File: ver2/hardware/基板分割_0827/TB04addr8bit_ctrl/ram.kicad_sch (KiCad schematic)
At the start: 6 parts, among them U1101 6116, U1102 74HC244, U1103 74HC244

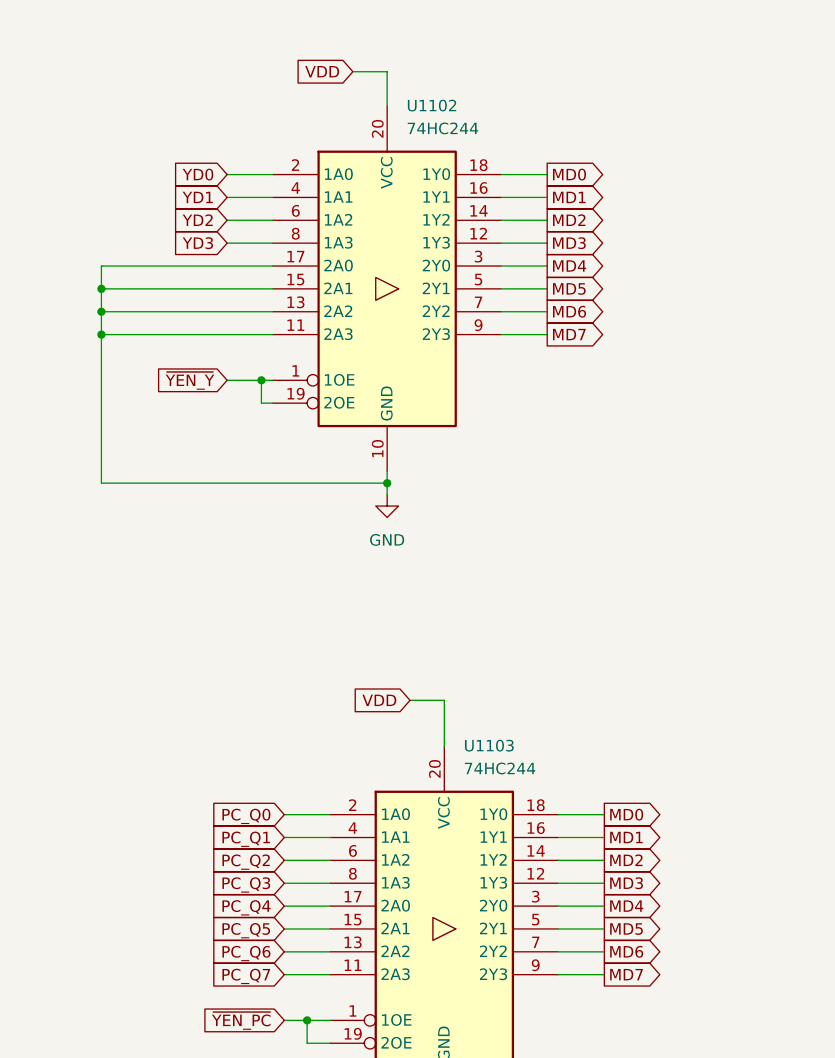
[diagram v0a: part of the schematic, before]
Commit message: ver2: 制御板のピン割当(案C)を適用(6IC・44ピン入替で交差-17.7%)
74HC244×3(U1102/U1103/U1402)・74HC157×3(U101/U401/U404)でバスのビット順を入替。
検証は全項目合格＝変化は44パッドのみ・244の(A,Y)対と157の(A,B,Y)三つ組は集合一致・
制御ピン不変・ネットの構成部品変化0・DRC/schematic parityはHEADと項目単位で完全一致。
HPWL +0.16%(15,542→15,567mm)。配置と外形は不動。

Co-Authored-By: Claude Opus 5 <noreply@anthropic.com>
Claude-Session: https://claude.ai/code/session_01FHQyZznjPPN9g6quxMNLGo
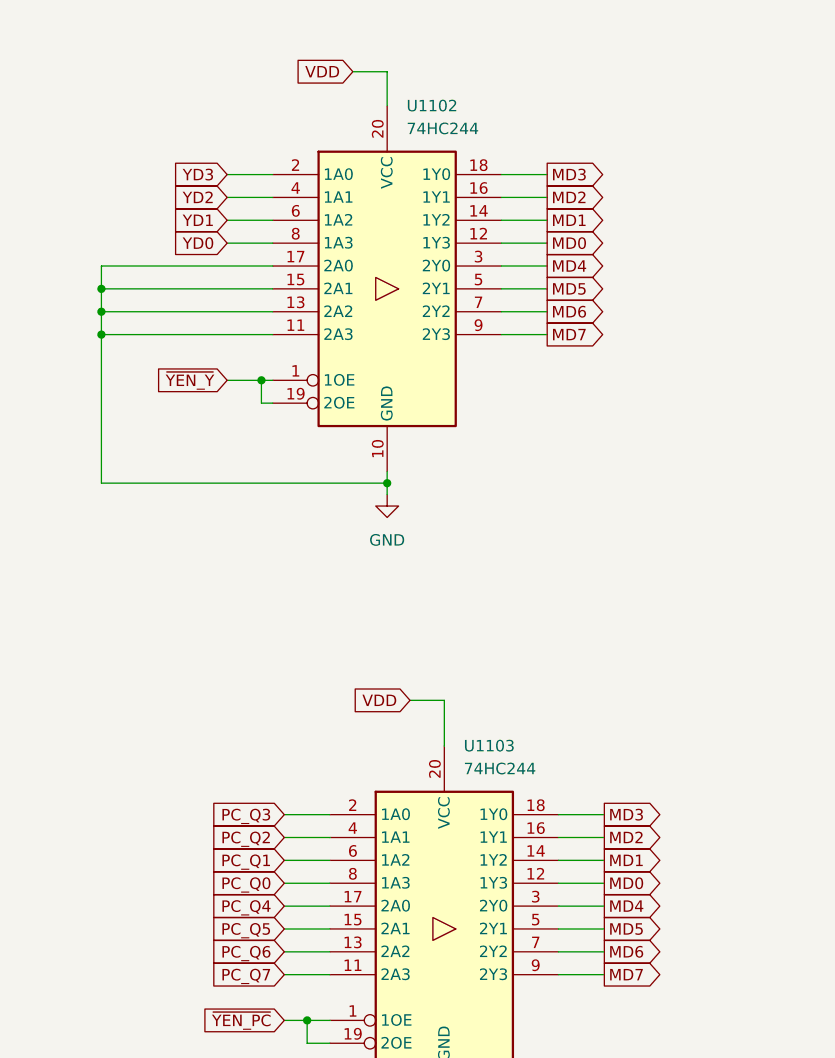
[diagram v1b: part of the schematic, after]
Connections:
- net MD0: now also U1102.12 (1Y3), U1103.12 (1Y3); no longer U1102.18 (1Y0), U1103.18 (1Y0)
- net MD1: now also U1102.14 (1Y2), U1103.14 (1Y2); no longer U1102.16 (1Y1), U1103.16 (1Y1)
- net MD2: now also U1102.16 (1Y1), U1103.16 (1Y1); no longer U1102.14 (1Y2), U1103.14 (1Y2)
- net MD3: now also U1102.18 (1Y0), U1103.18 (1Y0); no longer U1102.12 (1Y3), U1103.12 (1Y3)
- net PC_Q0: now also U1103.8 (1A3); no longer U1103.2 (1A0)
- net PC_Q1: now also U1103.6 (1A2); no longer U1103.4 (1A1)
- net PC_Q2: now also U1103.4 (1A1); no longer U1103.6 (1A2)
- net PC_Q3: now also U1103.2 (1A0); no longer U1103.8 (1A3)
- net YD0: now also U1102.8 (1A3); no longer U1102.2 (1A0)
- net YD1: now also U1102.6 (1A2); no longer U1102.4 (1A1)
- net YD2: now also U1102.4 (1A1); no longer U1102.6 (1A2)
- net YD3: now also U1102.2 (1A0); no longer U1102.8 (1A3)

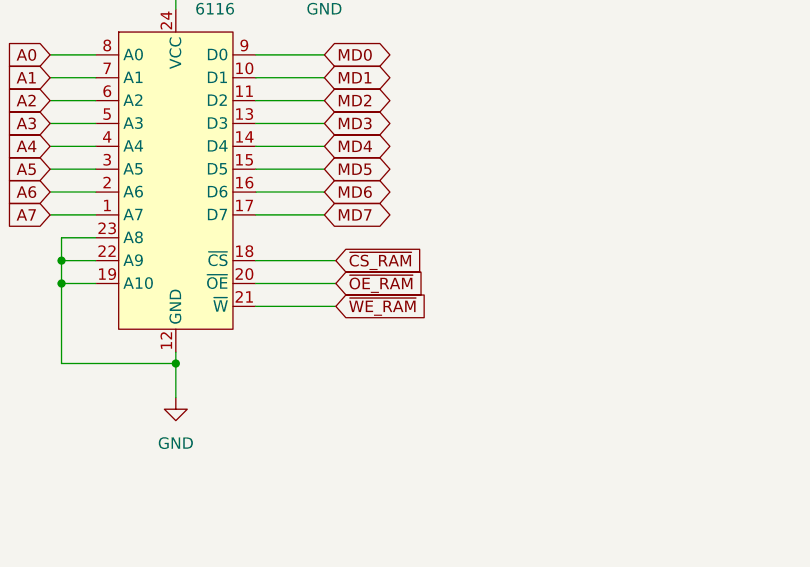
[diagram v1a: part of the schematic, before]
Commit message: ver2: シート15のゲートを6パッケージに整理(74HC08を1枚削除)
~OE_RAM を WR 直結にし(6116は /CE で出力がゲートされるため)、
RAM_STK_SEL と CS_RAM を ~CS_RAM=NAND3(P2,~P5,EXE) 1個にまとめ、
WR_EXE を NAND+INV に置き換えて AND 4つを U1503 へ集約。
U1507(74HC08)と C1502 を削除。7パッケージ27ゲート→6パッケージ25ゲート。

検証=HEADとのパッド-ネット署名比較で変化27パッド・部品103→101・
増えたネットなし・回路図↔PCBの不整合0。PCBはネットリスト同期済み。

Co-Authored-By: Claude Opus 5 <noreply@anthropic.com>
Claude-Session: https://claude.ai/code/session_012fBwfnqwV8TxUeD3onaDK6
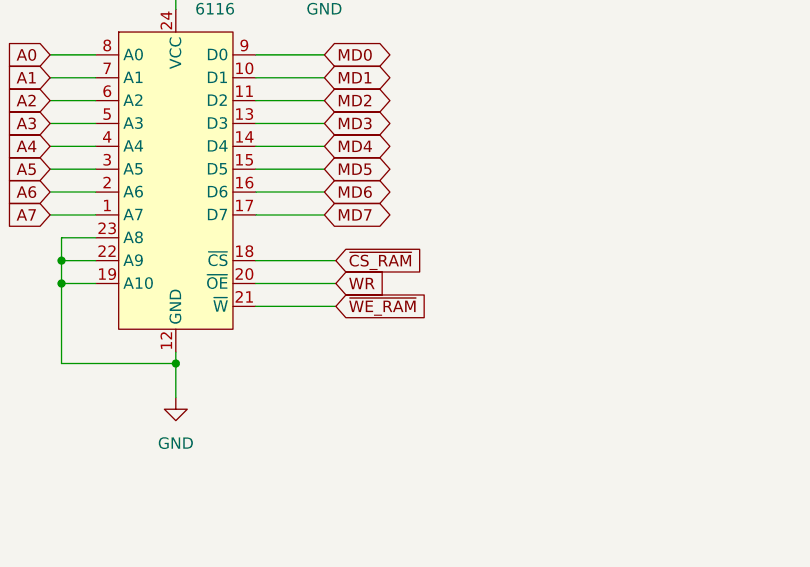
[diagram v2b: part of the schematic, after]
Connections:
- net ~{OE_RAM} renamed WR
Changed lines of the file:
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@@
 		)
 	)
-	(global_label "~{OE_RAM}"
+	(global_label "WR"
 		(shape input)
 		(at 95.25 68.58 0)
@@
 		)
 		(property "Intersheetrefs" "${INTERSHEET_REFS}"
-			(at 105.4923 68.58 0)
+			(at 100.9566 68.58 0)
 			(show_name no)
 			(do_not_autoplace no)
